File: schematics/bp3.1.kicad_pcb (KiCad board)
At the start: 2 copper layers, 47.6 x 31.3 mm, 26 parts, among them J1 Left Pin Strip, J2 Right Pin Strip, J3 I/O Pin Strip, SW1 Power Switch, U1 TPS61220DCK, U2 LM321

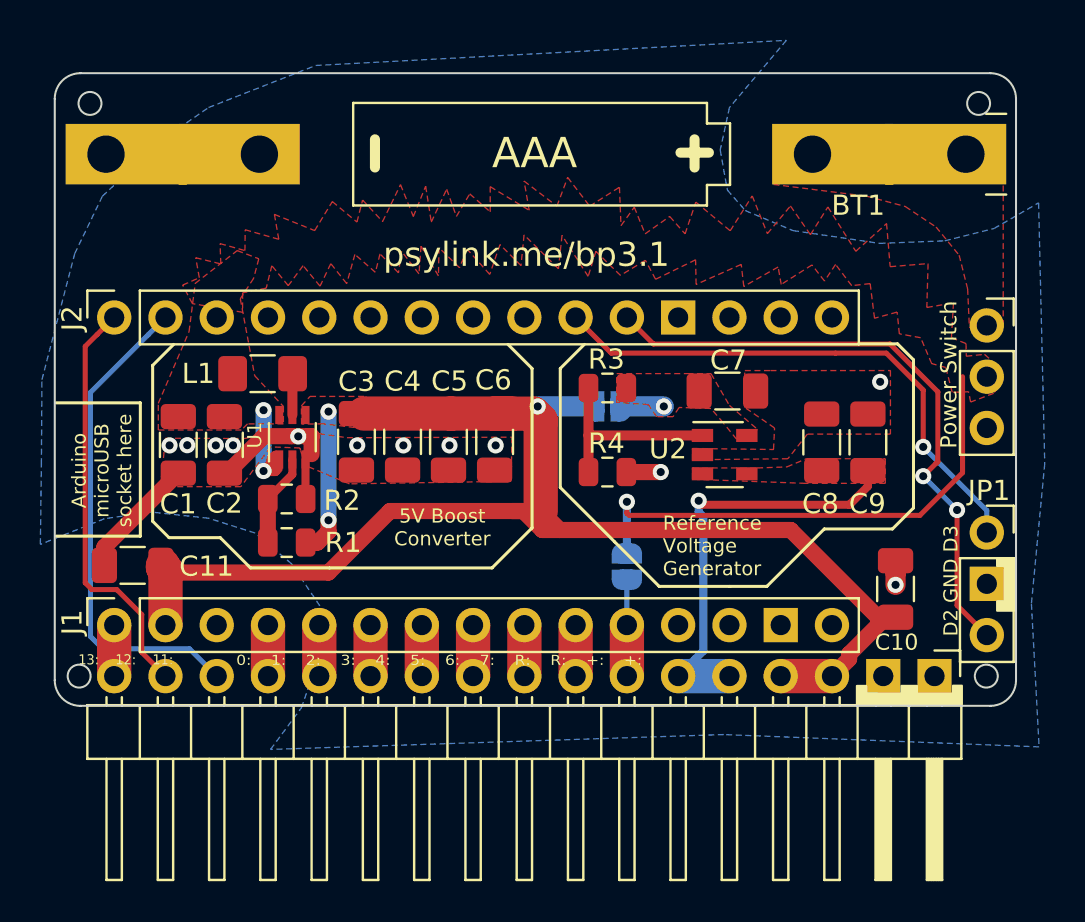
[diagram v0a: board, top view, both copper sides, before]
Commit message: Larger pads on bp3.1 for easier soldering (fixes #8)
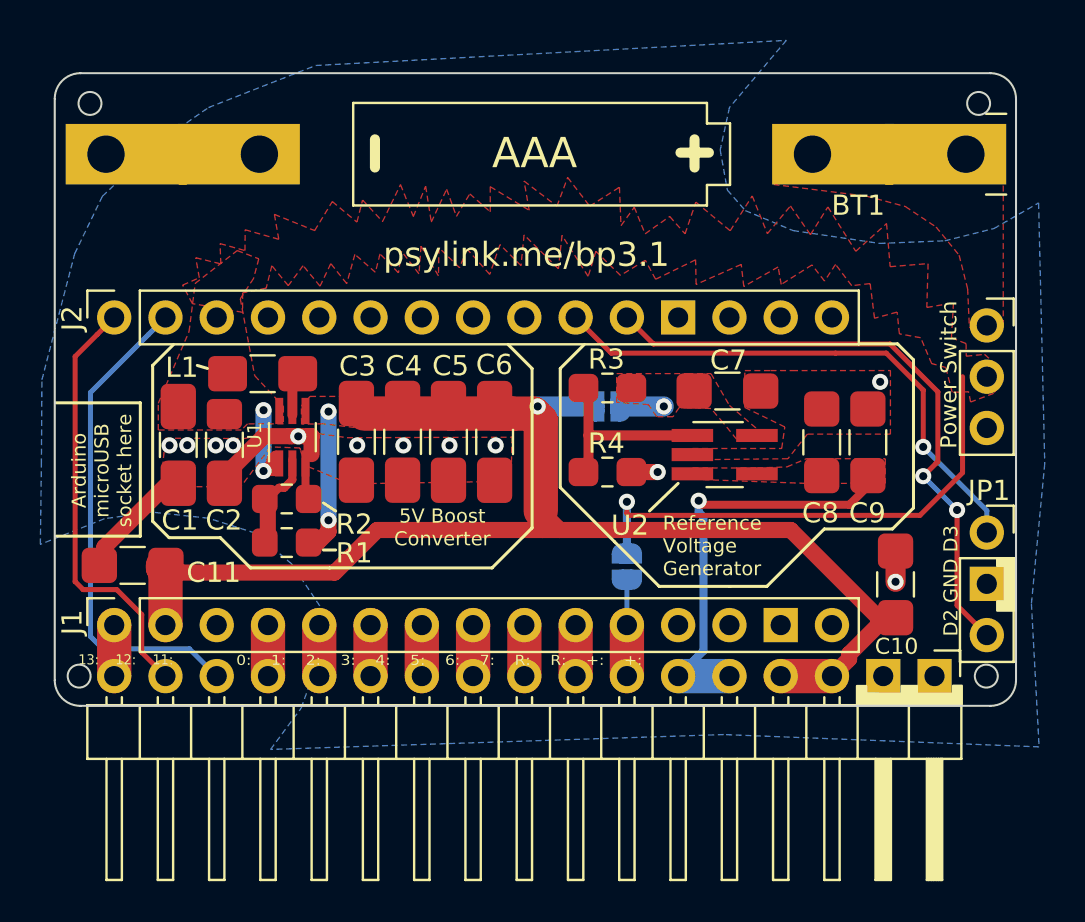
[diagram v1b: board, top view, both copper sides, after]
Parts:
- moved C10 0.23 mm to (64.8, 48.4)
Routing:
- net /V+: track 78.1 -> 75.9 mm
- net /D12: track 20.7 -> 21.4 mm

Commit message: updated/finalized bp3.1 (makes room for 1210 package inductance)
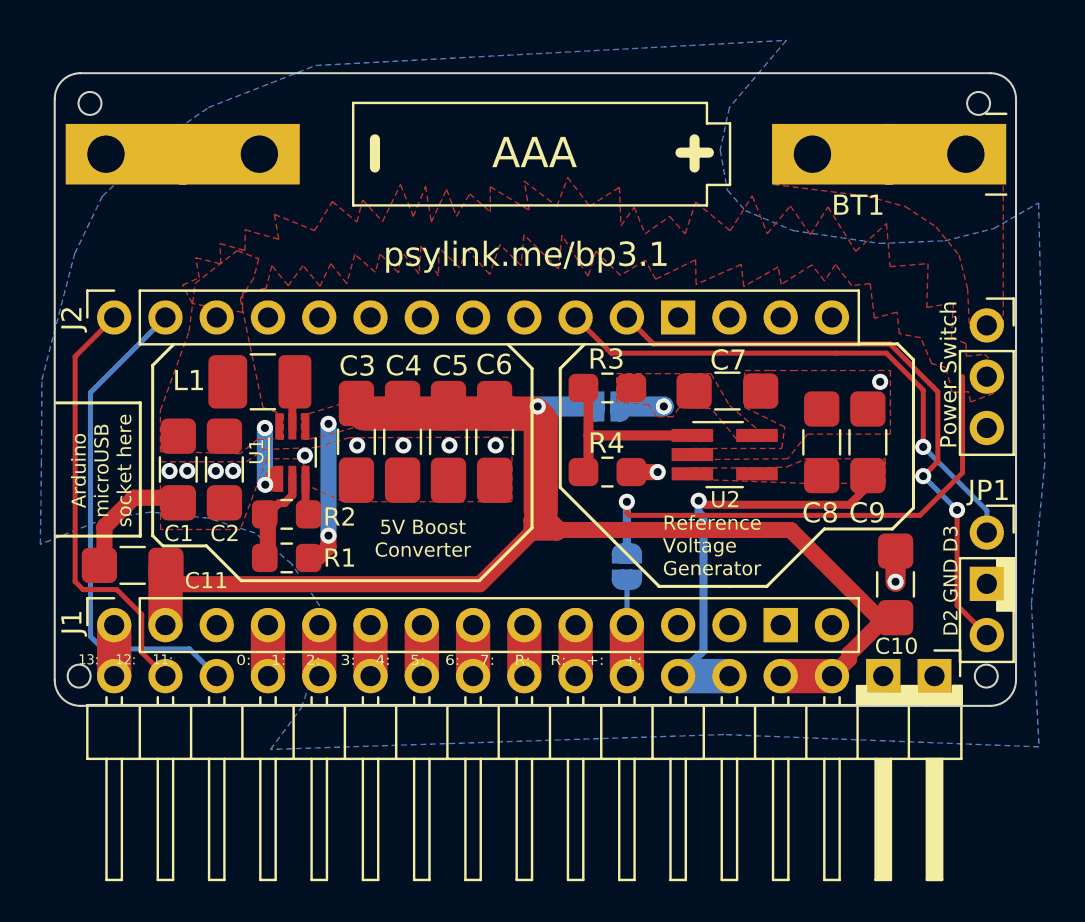
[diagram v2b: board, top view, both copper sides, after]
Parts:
- L1: footprint Inductor_SMD:L_1206_3216Metric_Pad1.42x1.75mm_HandSolder -> Inductor_SMD:L_1210_3225Metric_Pad1.42x2.65mm_HandSolder
- moved C1 1.22 mm to (29.2, 42.7)
- moved C2 1.22 mm to (31.5, 42.7)
- moved R1 0.76 mm to (34.6, 47.1)
- moved R2 0.76 mm to (34.6, 45.0)
- moved U1 0.76 mm to (34.9, 41.9)
- moved L1 0.40 mm to (33.4, 38.4)
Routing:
- net /GND: track 23.7 -> 17.9 mm
- net /V+: track 75.9 -> 77.5 mm
- net /Vbat: track 30.5 -> 30.0 mm
